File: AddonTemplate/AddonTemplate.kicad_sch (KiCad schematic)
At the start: 3 parts

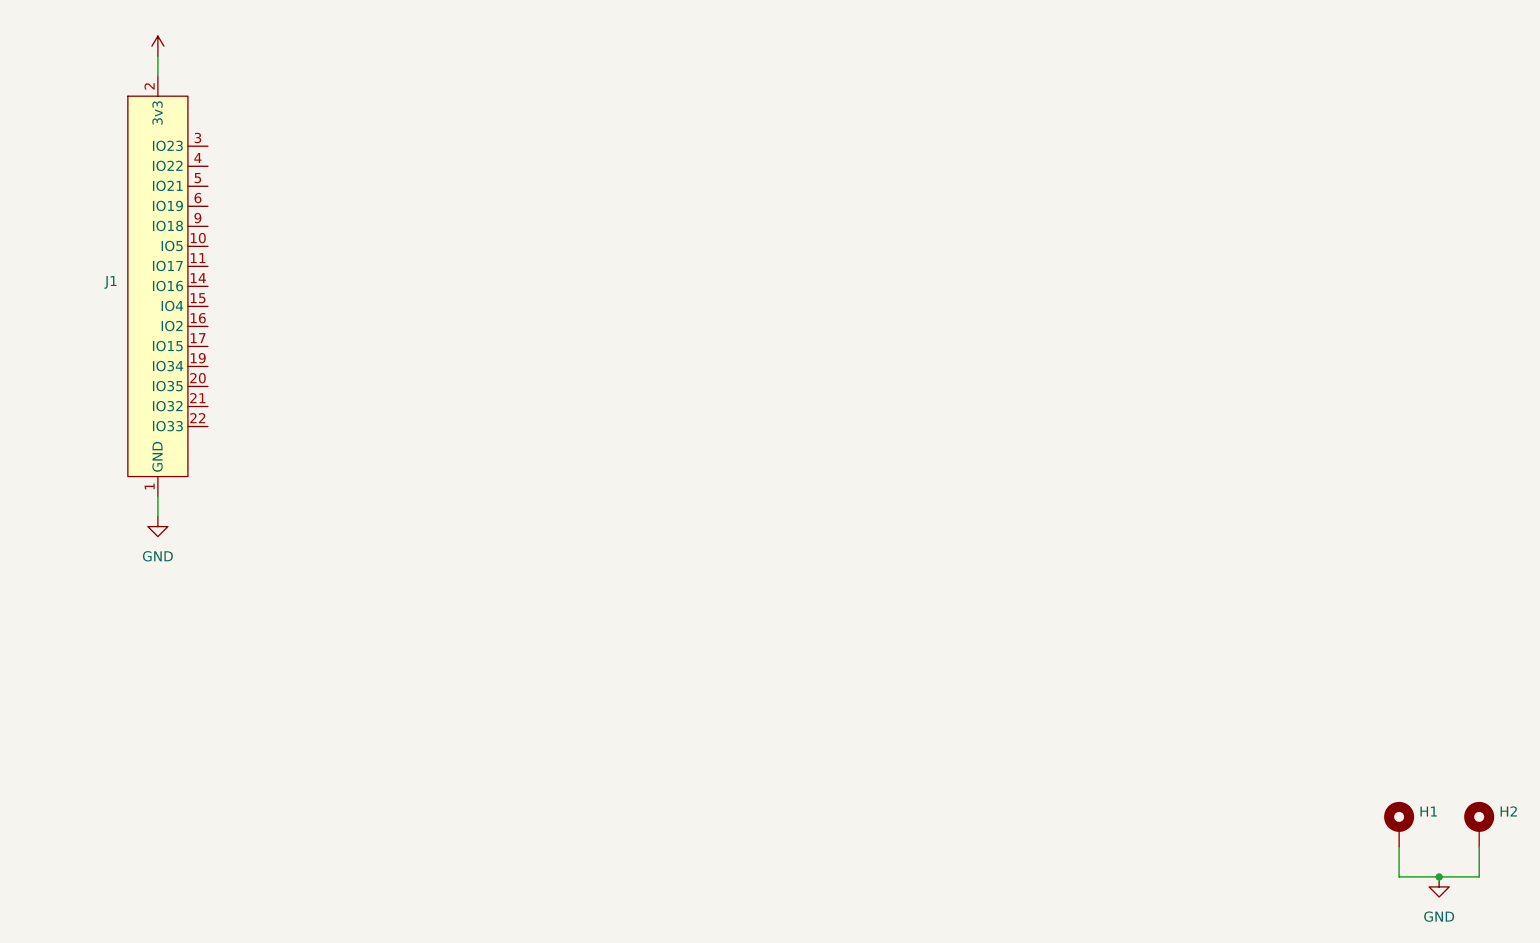
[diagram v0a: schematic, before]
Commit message: Adapts addon template to new version of the addon connector
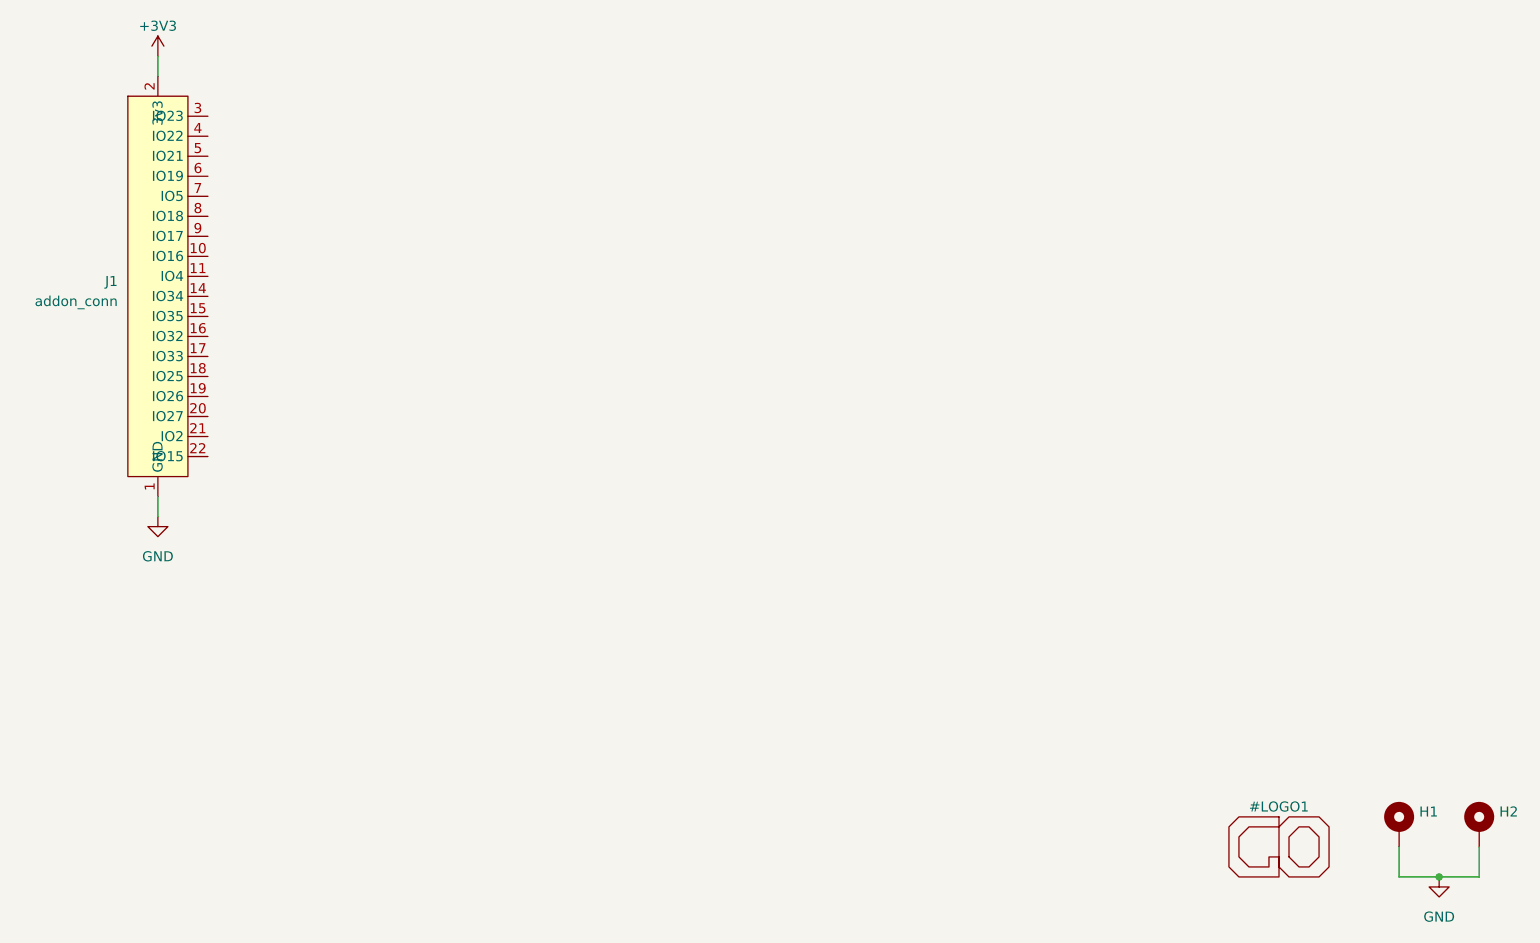
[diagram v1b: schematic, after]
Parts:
- J1: value (none) -> addon_conn; footprint (none) -> GameOver:Addon_conn_TXGA_FFC05036-24SBD113W5M_1x24_P0.50mm_Horizontal
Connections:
- net +3V3: no longer J1.8 (3v3)
- net GND: no longer J1.18 (GND), J1.7 (GND)
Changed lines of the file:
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@@
     (pin "1")
+  )
+  (symbol (lib_id "GameOver:GameOver_logo") (at 251.46 144.78 0) (unit 1)
+    (in_bom no) (on_board yes) (fields_autoplaced)
+    (property "Reference" "#LOGO1" (id 0) (at 251.46 139.7 0)
+      (effects (font (size 1.27 1.27)))
+    )
+    (property "Value" "" (id 1) (at 251.46 151.13 0)
+      (effects (font (size 1.27 1.27)) hide)
+    )
+    (property "Footprint" "" (id 2) (at 251.46 144.78 0)
+      (effects (font (size 1.27 1.27)) hide)
+    )
+    (property "Datasheet" "" (id 3) (at 251.46 144.78 0)
+      (effects (font (size 1.27 1.27)) hide)
+    )
   )
   (symbol (lib_id "GameOver:addon_conn") (at 109.22 73.66 0) (unit 1)
@@
       (effects (font (size 1.27 1.27)) (justify right))
     )
-    (property "Value" "" (id 1) (at 104.14 75.565 0)
+    (property "Value" "addon_conn" (id 1) (at 104.14 75.565 0)
       (effects (font (size 1.27 1.27)) (justify right))
     )
-    (property "Footprint" "" (id 2) (at 151.13 49.53 0)
+    (property "Footprint" "GameOver:Addon_conn_TXGA_FFC05036-24SBD113W5M_1x24_P0.50mm_Horizontal" (id 2) (at 151.13 49.53 0)
       (effects (font (size 1.27 1.27)) hide)
     )
@@
       (effects (font (size 1.27 1.27)) hide)
     )
-    (property "Value" "" (id 1) (at 109.22 40.64 0)
+    (property "Value" "+3V3" (id 1) (at 109.22 40.64 0)
       (effects (font (size 1.27 1.27)))
     )
@@
   )
   (symbol_instances
+    (path "/a720fc4e-11cc-40fc-995d-9cf7d6347fff"
+      (reference "#LOGO1") (unit 1) (value "GameOver_logo") (footprint "GameOver:logo_fcu")
+    )
     (path "/9688e065-eefa-4bd4-b63c-6f941775746e"
       (reference "#PWR01") (unit 1) (value "GND") (footprint "")
@@
     )
     (path "/b6197b6c-ed83-4343-8eb6-1b3b92c52240"
-      (reference "J1") (unit 1) (value "addon_conn") (footprint "GameOver:TXGA_FFC05036-24SBD113W5M_1x24_P0.50mm_Horizontal")
+      (reference "J1") (unit 1) (value "addon_conn") (footprint "GameOver:Addon_conn_TXGA_FFC05036-24SBD113W5M_1x24_P0.50mm_Horizontal")
     )
   )

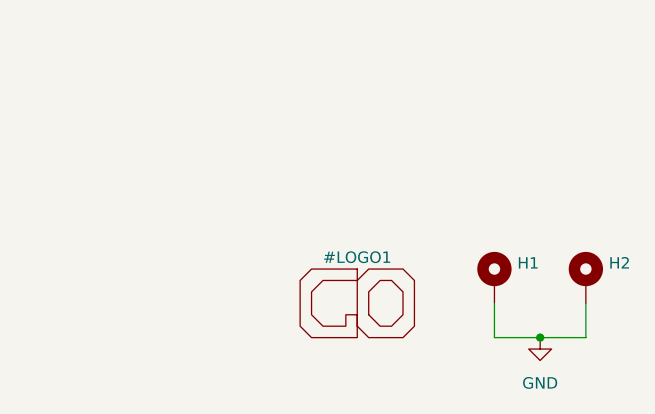
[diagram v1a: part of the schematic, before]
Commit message: Fixes logo schematics in the Addon template
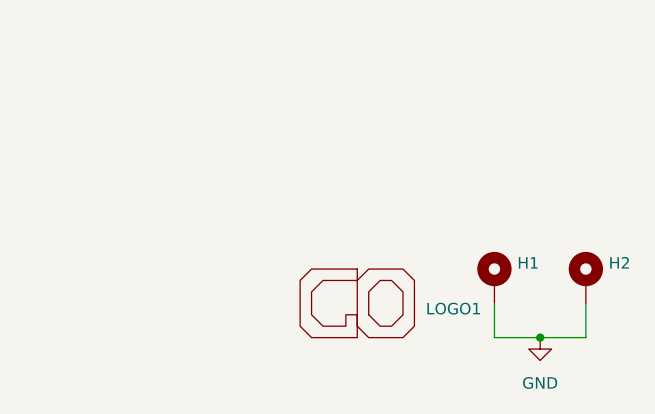
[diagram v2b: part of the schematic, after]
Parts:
- added LOGO1: GameOver_logo, GameOver:logo_fcu, symbol GameOver:GameOver_logo
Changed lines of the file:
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@@
   (symbol (lib_id "GameOver:GameOver_logo") (at 251.46 144.78 0) (unit 1)
     (in_bom no) (on_board yes) (fields_autoplaced)
-    (property "Reference" "#LOGO1" (id 0) (at 251.46 139.7 0)
-      (effects (font (size 1.27 1.27)))
+    (property "Reference" "LOGO1" (id 0) (at 259.08 145.415 0)
+      (effects (font (size 1.27 1.27)) (justify left))
     )
-    (property "Value" "" (id 1) (at 251.46 151.13 0)
+    (property "Value" "GameOver_logo" (id 1) (at 251.46 151.13 0)
       (effects (font (size 1.27 1.27)) hide)
     )
-    (property "Footprint" "" (id 2) (at 251.46 144.78 0)
+    (property "Footprint" "GameOver:logo_fcu" (id 2) (at 251.46 144.78 0)
       (effects (font (size 1.27 1.27)) hide)
     )
@@
   )
   (symbol_instances
-    (path "/a720fc4e-11cc-40fc-995d-9cf7d6347fff"
-      (reference "#LOGO1") (unit 1) (value "GameOver_logo") (footprint "GameOver:logo_fcu")
-    )
     (path "/9688e065-eefa-4bd4-b63c-6f941775746e"
       (reference "#PWR01") (unit 1) (value "GND") (footprint "")
@@
       (reference "J1") (unit 1) (value "addon_conn") (footprint "GameOver:Addon_conn_TXGA_FFC05036-24SBD113W5M_1x24_P0.50mm_Horizontal")
     )
+    (path "/a720fc4e-11cc-40fc-995d-9cf7d6347fff"
+      (reference "LOGO1") (unit 1) (value "GameOver_logo") (footprint "GameOver:logo_fcu")
+    )
   )

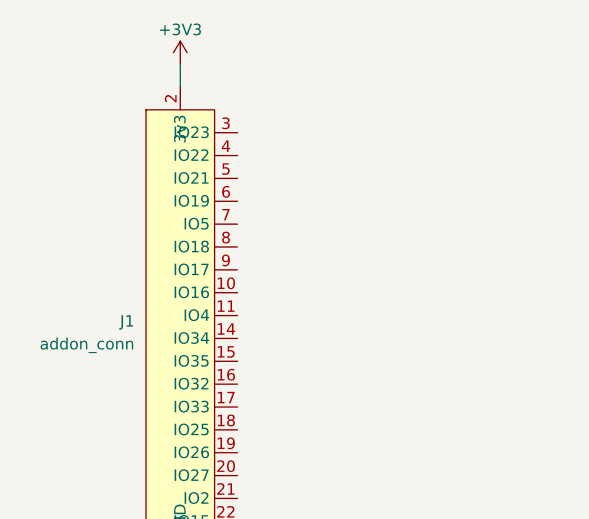
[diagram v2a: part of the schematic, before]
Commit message: Updates all add-on boards with fix introduced in 692041
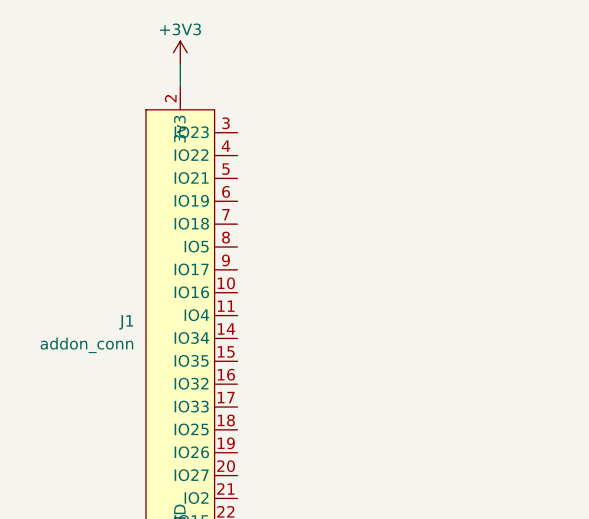
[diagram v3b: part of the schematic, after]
